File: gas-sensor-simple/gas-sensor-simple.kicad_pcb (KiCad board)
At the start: 2 copper layers, 97.8 x 99.1 mm, 47 parts, among them J1 RPi, J2 digital header, J3 digital header, J4 1x2, J5 1x2, J6 1x2, J7 1x2, U1 MQ-8, U10 RG LED, U12 LM393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

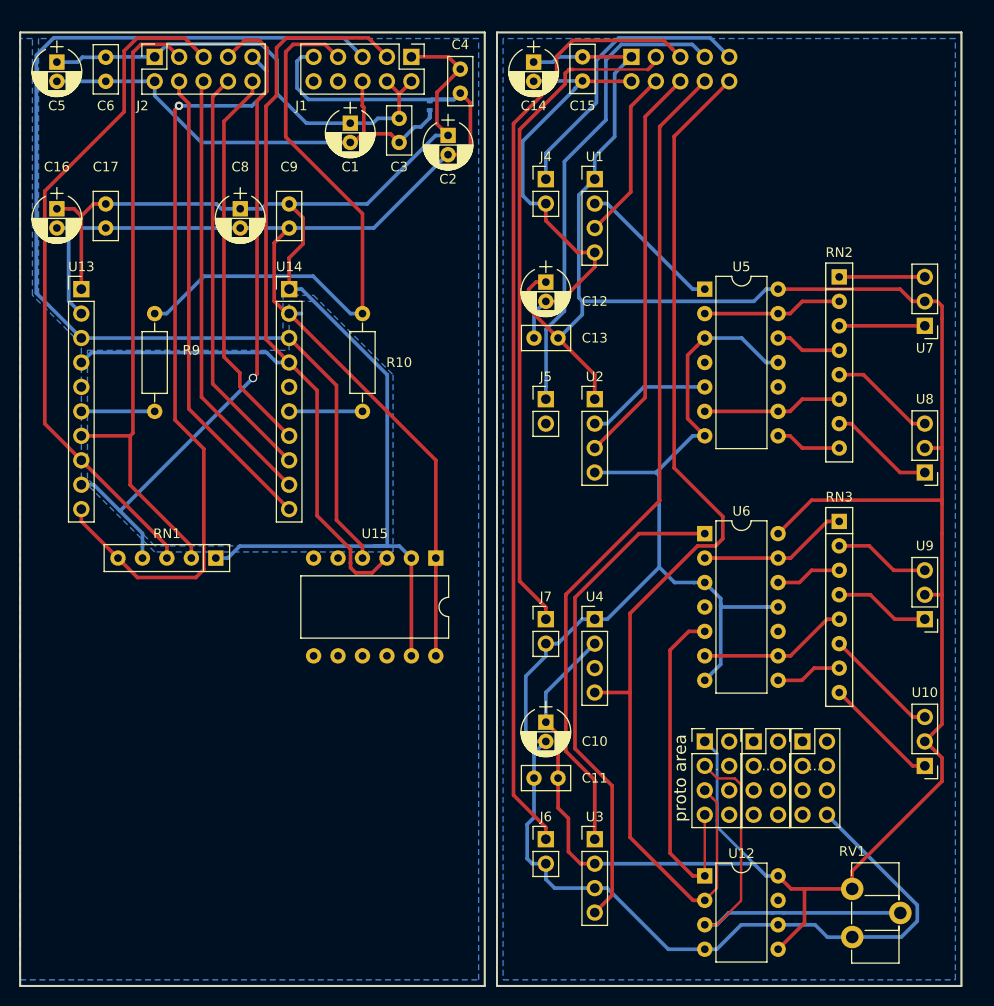
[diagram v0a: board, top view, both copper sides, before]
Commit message: Adjust board edges.
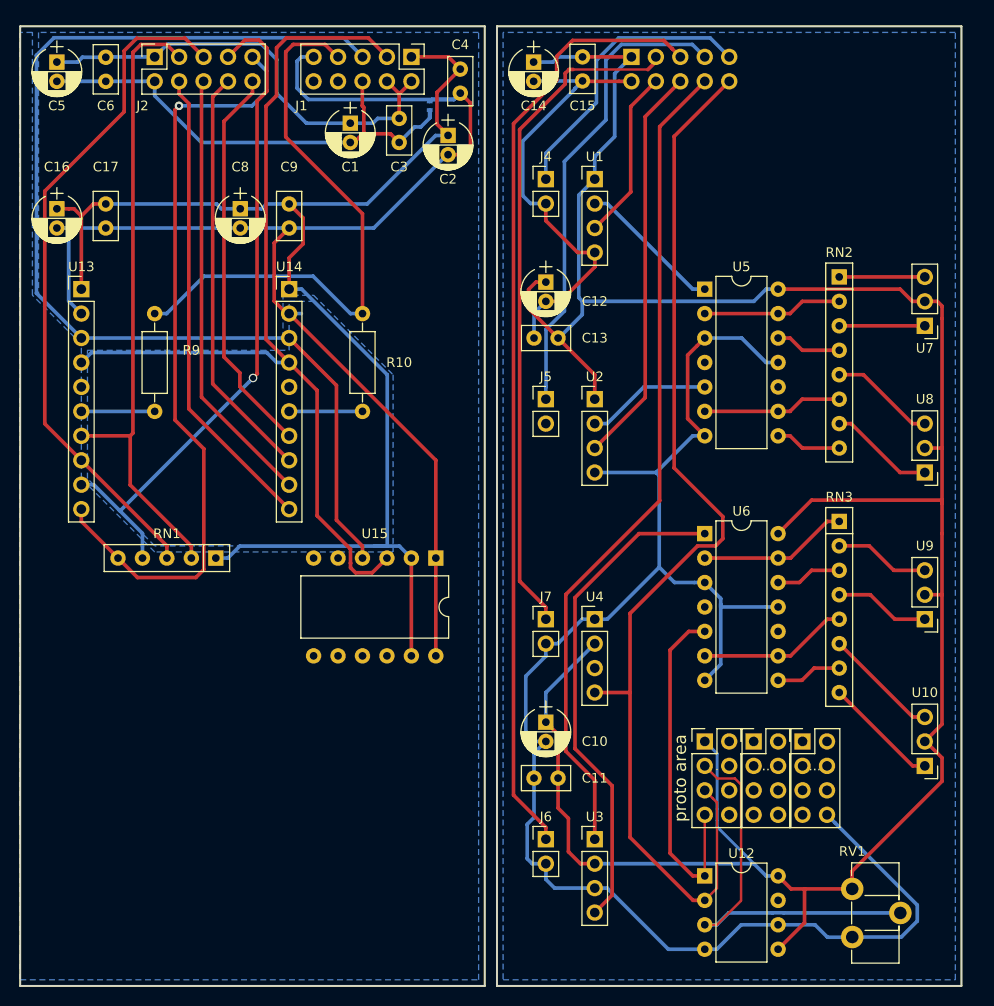
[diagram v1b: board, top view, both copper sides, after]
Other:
- board size 97.8 x 99.1 mm -> 97.8 x 99.7 mm
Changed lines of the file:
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@@
     )
   )
-  (gr_line (start 196.85 52.07) (end 148.59 52.07) (layer F.SilkS) (width 0.2))
-  (gr_line (start 196.85 151.13) (end 196.85 52.07) (layer F.SilkS) (width 0.2))
+  (gr_line (start 196.85 51.435) (end 148.59 51.435) (layer F.SilkS) (width 0.2))
+  (gr_line (start 196.85 151.13) (end 196.85 51.435) (layer F.SilkS) (width 0.2))
   (gr_line (start 148.59 151.13) (end 196.85 151.13) (layer F.SilkS) (width 0.2))
-  (gr_line (start 148.59 52.07) (end 148.59 151.13) (layer F.SilkS) (width 0.2))
-  (gr_line (start 147.32 52.07) (end 99.06 52.07) (layer F.SilkS) (width 0.2))
-  (gr_line (start 147.32 151.13) (end 147.32 52.07) (layer F.SilkS) (width 0.2))
+  (gr_line (start 148.59 51.435) (end 148.59 151.13) (layer F.SilkS) (width 0.2))
+  (gr_line (start 147.32 51.435) (end 99.06 51.435) (layer F.SilkS) (width 0.2))
+  (gr_line (start 147.32 151.13) (end 147.32 51.435) (layer F.SilkS) (width 0.2))
   (gr_line (start 99.06 151.13) (end 147.32 151.13) (layer F.SilkS) (width 0.2))
-  (gr_line (start 99.06 52.07) (end 99.06 151.13) (layer F.SilkS) (width 0.2))
-  (gr_line (start 99.06 52.07) (end 147.32 52.07) (layer Edge.Cuts) (width 0.1))
+  (gr_line (start 99.06 51.435) (end 99.06 151.13) (layer F.SilkS) (width 0.2))
+  (gr_line (start 99.06 51.435) (end 147.32 51.435) (layer Edge.Cuts) (width 0.1))
   (gr_line (start 148.59 151.13) (end 196.85 151.13) (layer Edge.Cuts) (width 0.1))
   (gr_line (start 99.06 151.13) (end 147.32 151.13) (layer Edge.Cuts) (width 0.1))
-  (gr_line (start 147.32 52.07) (end 147.32 151.13) (layer Edge.Cuts) (width 0.1))
-  (gr_line (start 148.59 52.07) (end 148.59 151.13) (layer Edge.Cuts) (width 0.1))
-  (gr_line (start 99.06 52.07) (end 99.06 151.13) (layer Edge.Cuts) (width 0.1))
-  (gr_line (start 196.85 52.07) (end 196.85 151.13) (layer Edge.Cuts) (width 0.1))
-  (gr_line (start 148.59 52.07) (end 196.85 52.07) (layer Edge.Cuts) (width 0.1))
+  (gr_line (start 147.32 51.435) (end 147.32 151.13) (layer Edge.Cuts) (width 0.1))
+  (gr_line (start 148.59 51.435) (end 148.59 151.13) (layer Edge.Cuts) (width 0.1))
+  (gr_line (start 99.06 51.435) (end 99.06 151.13) (layer Edge.Cuts) (width 0.1))
+  (gr_line (start 196.85 51.435) (end 196.85 151.13) (layer Edge.Cuts) (width 0.1))
+  (gr_line (start 148.59 51.435) (end 196.85 51.435) (layer Edge.Cuts) (width 0.1))
   (gr_text "proto area" (at 167.64 129.54 90) (layer F.SilkS)
     (effects (font (size 1.27 1.27) (thickness 0.127)))
@@
     (polygon
       (pts
-        (xy 100.965 52.705) (xy 100.965 79.375) (xy 105.41 83.82) (xy 126.365 83.82) (xy 126.365 79.375)
+        (xy 100.965 52.07) (xy 100.965 79.375) (xy 105.41 83.82) (xy 126.365 83.82) (xy 126.365 79.375)
         (xy 129.54 79.375) (xy 137.795 87.63) (xy 137.795 106.045) (xy 113.03 106.045) (xy 105.41 98.425)
-        (xy 105.41 84.455) (xy 100.33 79.375) (xy 100.33 52.705) (xy 99.06 52.705) (xy 99.06 150.495)
-        (xy 146.685 150.495) (xy 146.685 52.705)
+        (xy 105.41 84.455) (xy 100.33 79.375) (xy 100.33 52.07) (xy 99.06 52.07) (xy 99.06 150.495)
+        (xy 146.685 150.495) (xy 146.685 52.07)
       )
     )
@@
     (polygon
       (pts
-        (xy 196.215 52.705) (xy 149.225 52.705) (xy 149.225 150.495) (xy 196.215 150.495)
+        (xy 196.215 52.07) (xy 149.225 52.07) (xy 149.225 150.495) (xy 196.215 150.495)
       )
     )

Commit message: Adjust board positions to align common edge.
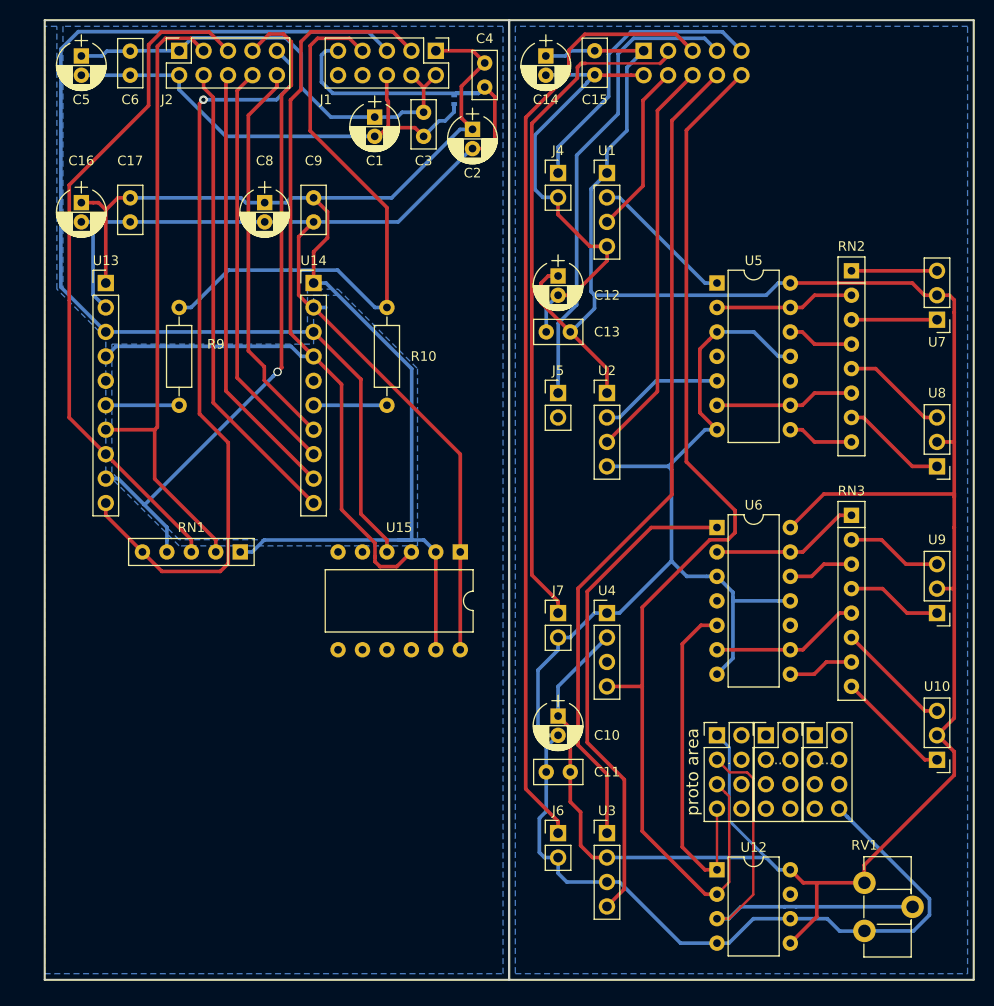
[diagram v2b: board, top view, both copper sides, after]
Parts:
- moved C2 2.62 mm to (146.1, 62.1)
- moved J1 2.62 mm to (142.2, 54.0)
- moved JP1 2.62 mm to (144.1, 59.1)
- moved RN1 2.62 mm to (121.9, 106.0)
- moved U13 2.62 mm to (108.0, 78.1)
- moved C16 2.62 mm to (105.4, 69.8)
- moved C17 2.62 mm to (110.5, 71.8)
- moved C4 2.62 mm to (147.3, 57.7)
- moved C8 2.62 mm to (124.5, 69.8)
- moved C9 2.62 mm to (129.5, 71.8)
- moved U15 2.62 mm to (144.8, 106.0)
- moved C1 2.62 mm to (135.9, 60.9)
- moved C3 2.62 mm to (141.0, 62.9)
- moved C5 2.62 mm to (105.4, 54.5)
- moved C6 2.62 mm to (110.5, 56.5)
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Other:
- board size 97.8 x 99.7 mm -> 96.5 x 99.7 mm
